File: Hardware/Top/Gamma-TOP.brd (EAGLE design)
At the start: 38 x 38 mm, 58 parts, among them SW1 SWITCH.MOM, SW2 SWITCH.MOM, U1 FT231XS, U3 NRF52832_MODULE_MDBT42, Y1 32.768kHz

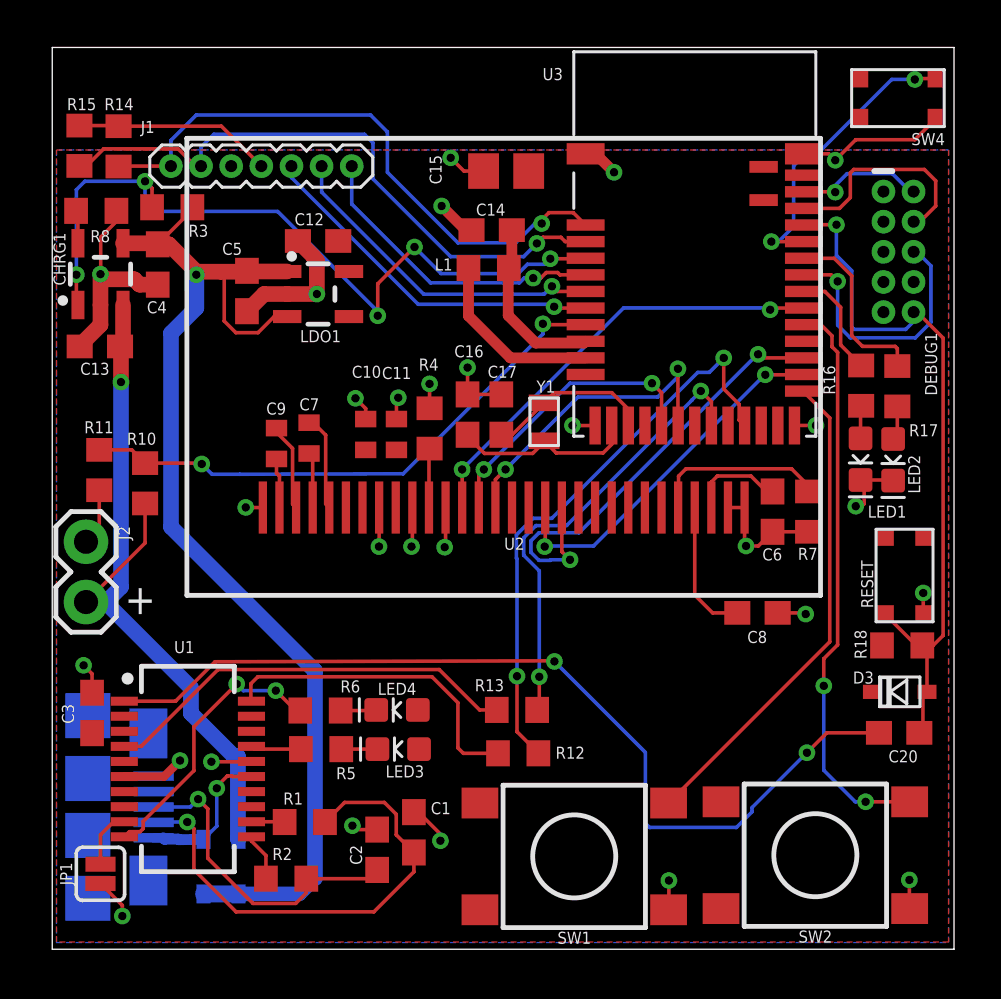
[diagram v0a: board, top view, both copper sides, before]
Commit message: Updated file names and completed preliminary BOM for each board
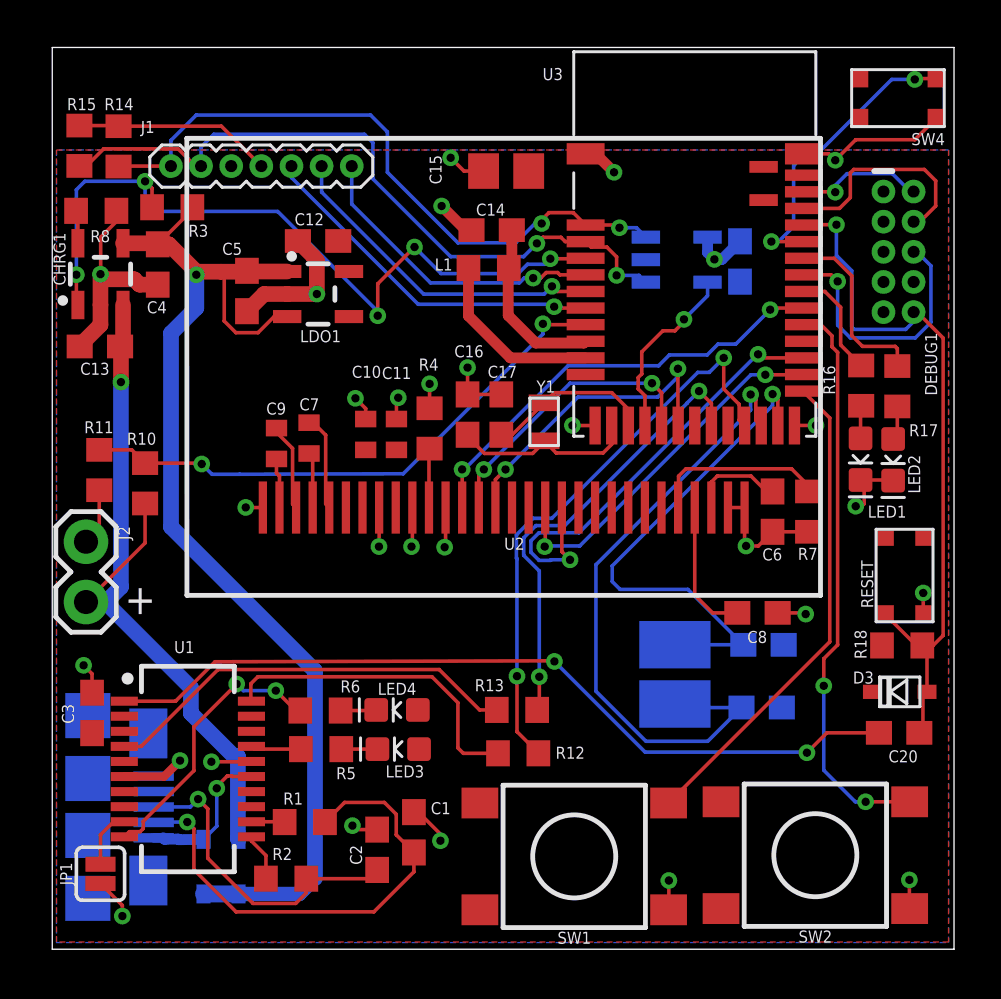
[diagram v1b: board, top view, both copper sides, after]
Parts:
- added C18, C21: 120p, LinnesLab-Passives:C0603
- added C19: 100n, LinnesLab-Passives:C0603
- added NFCANTENNA: 2.1 uH, NFC-Antenna:1462360151
- added U5: FT24C64A, LinnesLab-DigitalIC:SOT23-5
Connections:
- new net WP: U3.15, U5.5
- net 3.3V: now also C19.1, U5.4
- net GND: now also C18.2, C19.2, C21.2, U5.2
- net P0.09/NFC1: now also C18.1, NFCANTENNA.NFC1
- net P0.10/NFC2: now also C21.1, NFCANTENNA.NFC2
- net SCL: now also U5.1
- net SDA: now also U5.3
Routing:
- net P0.09/NFC1: track 0.00 -> 27.2 mm, vias 0 -> 1
- net P0.10/NFC2: track 0.00 -> 21.6 mm, vias 0 -> 1
- net WP: track 0.00 -> 7.67 mm, vias 0 -> 1
- net DTR: track 38.9 -> 34.4 mm
- net SCL: track 26.4 -> 30.1 mm, vias 1 -> 2
- net SDA: track 25.3 -> 28.0 mm, vias 1 -> 2
- net 3.3V: track 8.37 -> 10.8 mm, vias 0 -> 1
